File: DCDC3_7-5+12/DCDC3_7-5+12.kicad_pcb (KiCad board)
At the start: 2 copper layers, 63.5 x 75.8 mm, 34 parts, among them J1 FAN, Q1 CSD16323Q3, T1 + 3.7V -, T2 + 12V -, T3 + 5V -, U1 LM3488, U2 XL6009

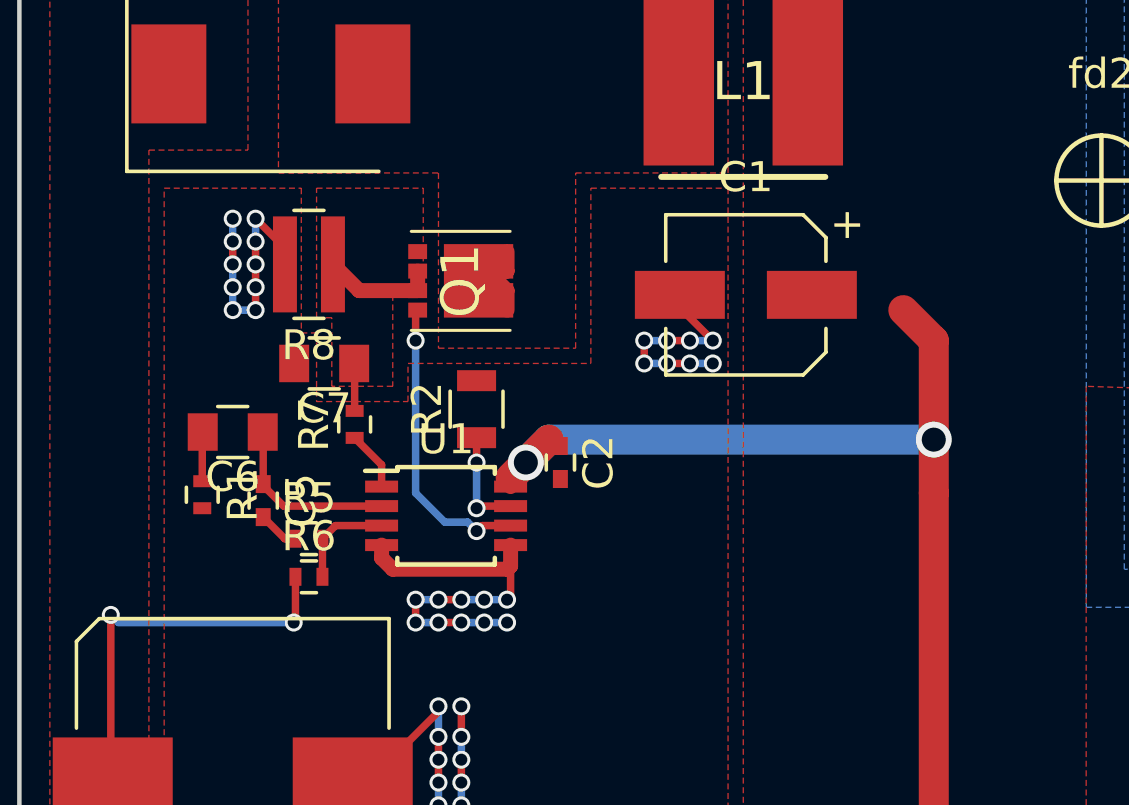
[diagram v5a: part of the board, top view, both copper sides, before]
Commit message: Final version of aux 5v and 12v power supply.
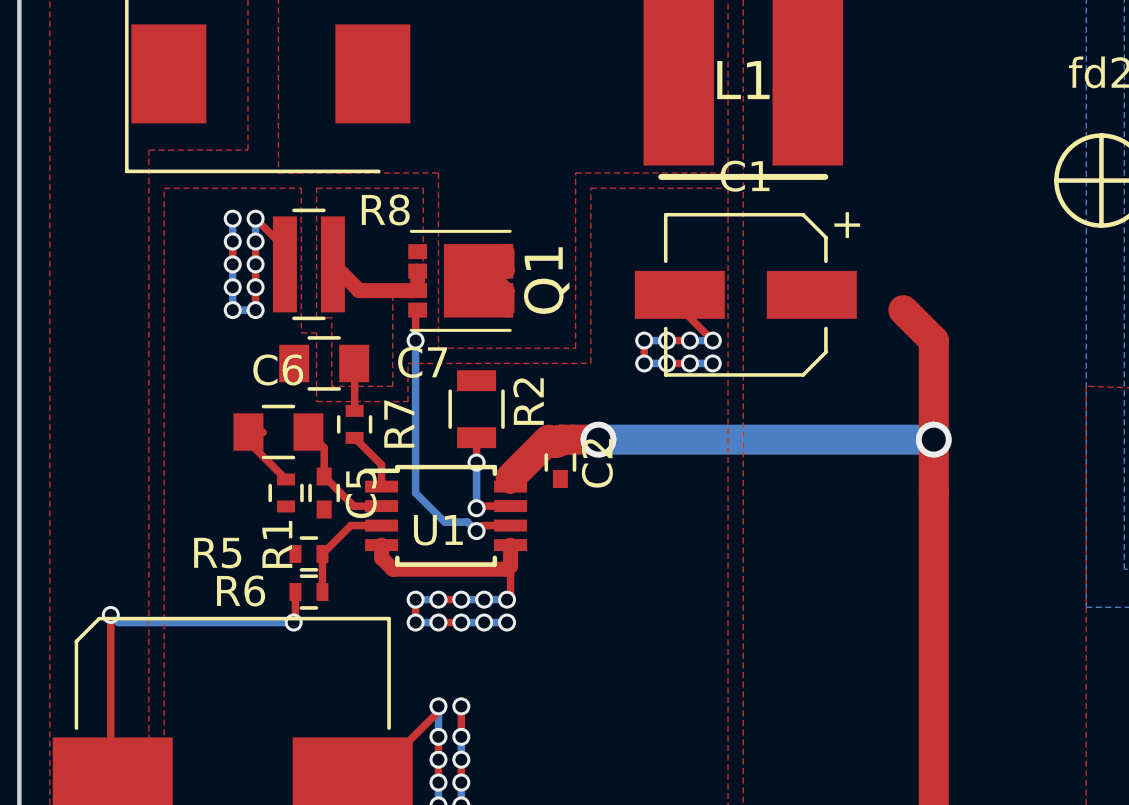
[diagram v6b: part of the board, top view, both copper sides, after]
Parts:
- moved R1 2.79 mm to (110.5, 105.4)
- moved C5 2.05 mm to (111.8, 105.4)
- moved C6 1.52 mm to (110.2, 103.4)
- moved R6 0.51 mm to (111.3, 108.7)
- moved R5 0.51 mm to (111.3, 107.4)
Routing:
- net Net-(C5-Pad1): track 6.02 -> 4.02 mm
- net GND: track 75.9 -> 74.5 mm
- net /DCDC 3.7 - 12/3.7V: track 93.6 -> 92.8 mm
- net /DCDC 3.7 - 12/12V: track 13.1 -> 12.6 mm
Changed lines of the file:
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@@
 (kicad_pcb (version 4) (host pcbnew 4.0.7+dfsg1-1ubuntu2)
   (general
-    (links 0)
+    (links 62)
     (no_connects 0)
     (area 101.524999 63.424999 165.175001 139.375001)
     (thickness 1.6)
     (drawings 12)
-    (tracks 204)
+    (tracks 207)
     (zones 0)
     (modules 34)
@@
   )
   (module Resistors_SMD:R_0402 (layer F.Cu)
-    (at 107.696 105.468 270)
+    (at 110.49 105.41 270)
     (descr "Resistor SMD 0402, reflow soldering, Vishay (see dcrcw.pdf)")
     (tags "resistor 0402")
     (attr smd)
-    (fp_text reference R1 (at 0 -1.35 270) (layer F.SilkS)
+    (fp_text reference R1 (at 1.72 0.254 270) (layer F.SilkS)
       (effects (font (size 1 1) (thickness 0.15)))
     )
@@
     (tags "MOSFET (N-Channel)")
     (attr smd)
-    (fp_text reference Q1 (at 0 0 270) (layer F.SilkS)
+    (fp_text reference Q1 (at -0.041 -2.815 270) (layer F.SilkS)
       (effects (font (size 1.27 1.27) (thickness 0.254)))
     )
@@
   )
   (module Capacitors_SMD:C_0402 (layer F.Cu)
-    (at 109.728 105.664 270)
+    (at 111.76 105.41 270)
     (descr "Capacitor SMD 0402, reflow soldering, AVX (see smccp.pdf)")
     (tags "capacitor 0402")
@@
   )
   (module Capacitors_SMD:C_0805 (layer F.Cu)
-    (at 108.712 103.378 180)
+    (at 110.236 103.378 180)
     (descr "Capacitor SMD 0805, reflow soldering, AVX (see smccp.pdf)")
     (tags "capacitor 0805")
     (attr smd)
-    (fp_text reference C6 (at 0 -1.5 180) (layer F.SilkS)
+    (fp_text reference C6 (at 0 2.032 180) (layer F.SilkS)
       (effects (font (size 1 1) (thickness 0.15)))
     )
@@
     (tags "capacitor 0805")
     (attr smd)
-    (fp_text reference C7 (at 0 -1.5 180) (layer F.SilkS)
+    (fp_text reference C7 (at -3.302 0 180) (layer F.SilkS)
       (effects (font (size 1 1) (thickness 0.15)))
     )
@@
     (tags "resistor 0805")
     (attr smd)
-    (fp_text reference R2 (at 0 -1.65 90) (layer F.SilkS)
+    (fp_text reference R2 (at 0.254 1.778 90) (layer F.SilkS)
       (effects (font (size 1 1) (thickness 0.15)))
     )
@@
   )
   (module Resistors_SMD:R_0402 (layer F.Cu)
-    (at 111.252 106.934)
+    (at 111.252 107.442)
     (descr "Resistor SMD 0402, reflow soldering, Vishay (see dcrcw.pdf)")
     (tags "resistor 0402")
     (attr smd)
-    (fp_text reference R5 (at 0 -1.35) (layer F.SilkS)
+    (fp_text reference R5 (at -3.048 0) (layer F.SilkS)
       (effects (font (size 1 1) (thickness 0.15)))
     )
@@
   )
   (module Resistors_SMD:R_0402 (layer F.Cu)
-    (at 111.252 108.204)
+    (at 111.252 108.712)
     (descr "Resistor SMD 0402, reflow soldering, Vishay (see dcrcw.pdf)")
     (tags "resistor 0402")
     (attr smd)
-    (fp_text reference R6 (at 0 -1.35) (layer F.SilkS)
+    (fp_text reference R6 (at -2.286 0) (layer F.SilkS)
       (effects (font (size 1 1) (thickness 0.15)))
     )
@@
     (tags "resistor 0402")
     (attr smd)
-    (fp_text reference R7 (at 0 -1.35 90) (layer F.SilkS)
+    (fp_text reference R7 (at 0 1.524 90) (layer F.SilkS)
       (effects (font (size 1 1) (thickness 0.15)))
     )
@@
     (tags "resistor 0612 ")
     (attr smd)
-    (fp_text reference R8 (at 0 -2.7 180) (layer F.SilkS)
+    (fp_text reference R8 (at -2.54 1.778 180) (layer F.SilkS)
       (effects (font (size 1 1) (thickness 0.15)))
     )
@@
     (tags "SSOP 0.65")
     (attr smd)
-    (fp_text reference U1 (at 0 -2.55) (layer F.SilkS)
+    (fp_text reference U1 (at -0.254 0.508) (layer F.SilkS)
       (effects (font (size 1 1) (thickness 0.15)))
     )
@@
   (gr_line (start 165.1 63.5) (end 165.1 139.3) (layer Edge.Cuts) (width 0.15))
   (gr_line (start 101.6 63.5) (end 165.1 63.5) (layer Edge.Cuts) (width 0.15))
-  (segment (start 119.244 103.632) (end 118.482 104.394) (width 1) (layer F.Cu) (net 1))
-  (segment (start 118.482 104.394) (end 117.974 104.902) (width 1) (layer F.Cu) (net 1))
-  (segment (start 119.244 103.632) (end 118.482 104.394) (width 1) (layer B.Cu) (net 1))
-  (segment (start 132.08 103.632) (end 119.244 103.632) (width 1) (layer B.Cu) (net 1))
-  (via (at 118.482 104.394) (size 1.2) (drill 0.8) (layers F.Cu B.Cu) (net 1))
+  (segment (start 120.904006 103.632) (end 120.904 103.632006) (width 1) (layer B.Cu) (net 1))
+  (segment (start 119.633994 103.632006) (end 120.055472 103.632006) (width 1) (layer F.Cu) (net 1))
+  (segment (start 132.08 103.632) (end 120.904006 103.632) (width 1) (layer B.Cu) (net 1))
+  (via (at 120.904 103.632006) (size 1.2) (drill 0.8) (layers F.Cu B.Cu) (net 1))
+  (segment (start 117.974 104.902) (end 119.152001 103.723999) (width 1) (layer F.Cu) (net 1))
+  (segment (start 120.055472 103.632006) (end 120.904 103.632006) (width 1) (layer F.Cu) (net 1))
+  (segment (start 119.542001 103.723999) (end 119.633994 103.632006) (width 1) (layer F.Cu) (net 1))
+  (segment (start 119.152001 103.723999) (end 119.542001 103.723999) (width 1) (layer F.Cu) (net 1))
+  (segment (start 119.335999 103.723999) (end 119.542001 103.723999) (width 1) (layer F.Cu) (net 1))
+  (segment (start 119.244 103.632) (end 119.335999 103.723999) (width 1) (layer F.Cu) (net 1))
   (via (at 132.08 103.632) (size 1.2) (drill 0.8) (layers F.Cu B.Cu) (net 1))
   (segment (start 119.634 103.844) (end 119.456 103.844) (width 0.25) (layer F.Cu) (net 1))
@@
   (segment (start 148.33 95.68) (end 145.03 95.68) (width 1) (layer F.Cu) (net 1))
   (segment (start 145.03 95.68) (end 144.78 95.93) (width 1) (layer F.Cu) (net 1))
+  (segment (start 110.802 108.712) (end 110.802 109.67) (width 0.25) (layer F.Cu) (net 2))
+  (segment (start 110.802 109.67) (end 110.744 109.728) (width 0.25) (layer F.Cu) (net 2))
   (segment (start 104.648 109.474) (end 104.648 114.744) (width 0.25) (layer F.Cu) (net 2))
   (segment (start 104.648 114.744) (end 104.712 114.808) (width 0.25) (layer F.Cu) (net 2))
@@
   (segment (start 104.902 109.728) (end 104.648 109.474) (width 0.25) (layer B.Cu) (net 2))
   (via (at 104.648 109.474) (size 0.6) (drill 0.4) (layers F.Cu B.Cu) (net 2))
-  (segment (start 110.802 108.204) (end 110.802 109.67) (width 0.25) (layer F.Cu) (net 2))
-  (segment (start 110.802 109.67) (end 110.744 109.728) (width 0.25) (layer F.Cu) (net 2))
   (via (at 110.744 109.728) (size 0.6) (drill 0.4) (layers F.Cu B.Cu) (net 2))
   (segment (start 153.67 133.35) (end 153.67 128.27) (width 1) (layer F.Cu) (net 3))
@@
   (segment (start 110.452 97.244) (end 109.474 96.266) (width 0.25) (layer F.Cu) (net 6))
   (via (at 109.474 96.266) (size 0.6) (drill 0.4) (layers F.Cu B.Cu) (net 6))
-  (segment (start 110.802 106.934) (end 110.448 106.934) (width 0.25) (layer F.Cu) (net 6))
-  (segment (start 110.448 106.934) (end 109.728 106.214) (width 0.25) (layer F.Cu) (net 6))
   (segment (start 113.674 107.147) (end 113.674 107.578) (width 0.5) (layer F.Cu) (net 6))
   (segment (start 117.871 107.95) (end 117.974 107.847) (width 0.5) (layer F.Cu) (net 6))
@@
   (segment (start 148.59 93.98) (end 148.33 93.98) (width 1) (layer F.Cu) (net 6))
   (segment (start 148.33 93.98) (end 148.33 93.72) (width 1) (layer F.Cu) (net 6))
-  (segment (start 109.728 105.114) (end 109.728 103.394) (width 0.25) (layer F.Cu) (net 7))
-  (segment (start 109.728 103.394) (end 109.712 103.378) (width 0.25) (layer F.Cu) (net 7))
-  (segment (start 113.674 105.847) (end 110.411 105.847) (width 0.25) (layer F.Cu) (net 7))
-  (segment (start 110.411 105.847) (end 109.728 105.164) (width 0.25) (layer F.Cu) (net 7))
-  (segment (start 109.728 105.164) (end 109.728 105.114) (width 0.25) (layer F.Cu) (net 7))
-  (segment (start 107.696 105.018) (end 107.696 103.394) (width 0.25) (layer F.Cu) (net 8))
-  (segment (start 107.696 103.394) (end 107.712 103.378) (width 0.25) (layer F.Cu) (net 8))
+  (segment (start 111.76 104.86) (end 112.747 105.847) (width 0.25) (layer F.Cu) (net 7))
+  (segment (start 112.747 105.847) (end 113.674 105.847) (width 0.25) (layer F.Cu) (net 7))
+  (segment (start 111.76 104.86) (end 111.76 103.902) (width 0.25) (layer F.Cu) (net 7))
+  (segment (start 111.76 103.902) (end 111.236 103.378) (width 0.25) (layer F.Cu) (net 7))
+  (segment (start 109.728 103.394) (end 109.712 103.378) (width 0.25) (layer F.Cu) (net 8))
+  (segment (start 110.49 104.96) (end 109.236 103.706) (width 0.25) (layer F.Cu) (net 8))
+  (segment (start 109.236 103.706) (end 109.236 103.378) (width 0.25) (layer F.Cu) (net 8))
   (segment (start 114.876 98.664) (end 112.926 98.664) (width 0.5) (layer F.Cu) (net 9))
   (segment (start 112.926 98.664) (end 112.052 97.79) (width 0.5) (layer F.Cu) (net 9))
@@
   (segment (start 116.911 105.847) (end 116.84 105.918) (width 0.25) (layer F.Cu) (net 12))
   (via (at 116.84 105.918) (size 0.6) (drill 0.4) (layers F.Cu B.Cu) (net 12))
-  (segment (start 111.702 106.934) (end 111.702 108.204) (width 0.25) (layer F.Cu) (net 13))
-  (segment (start 113.674 106.497) (end 112.139 106.497) (width 0.25) (layer F.Cu) (net 13))
-  (segment (start 112.139 106.497) (end 111.702 106.934) (width 0.25) (layer F.Cu) (net 13))
+  (segment (start 111.702 107.442) (end 112.647 106.497) (width 0.25) (layer F.Cu) (net 13))
+  (segment (start 112.647 106.497) (end 113.674 106.497) (width 0.25) (layer F.Cu) (net 13))
+  (segment (start 111.702 108.712) (end 111.702 107.442) (width 0.25) (layer F.Cu) (net 13))
   (segment (start 113.674 105.197) (end 113.674 104.472) (width 0.25) (layer F.Cu) (net 14))
   (segment (start 113.674 104.472) (end 112.776 103.574) (width 0.25) (layer F.Cu) (net 14))

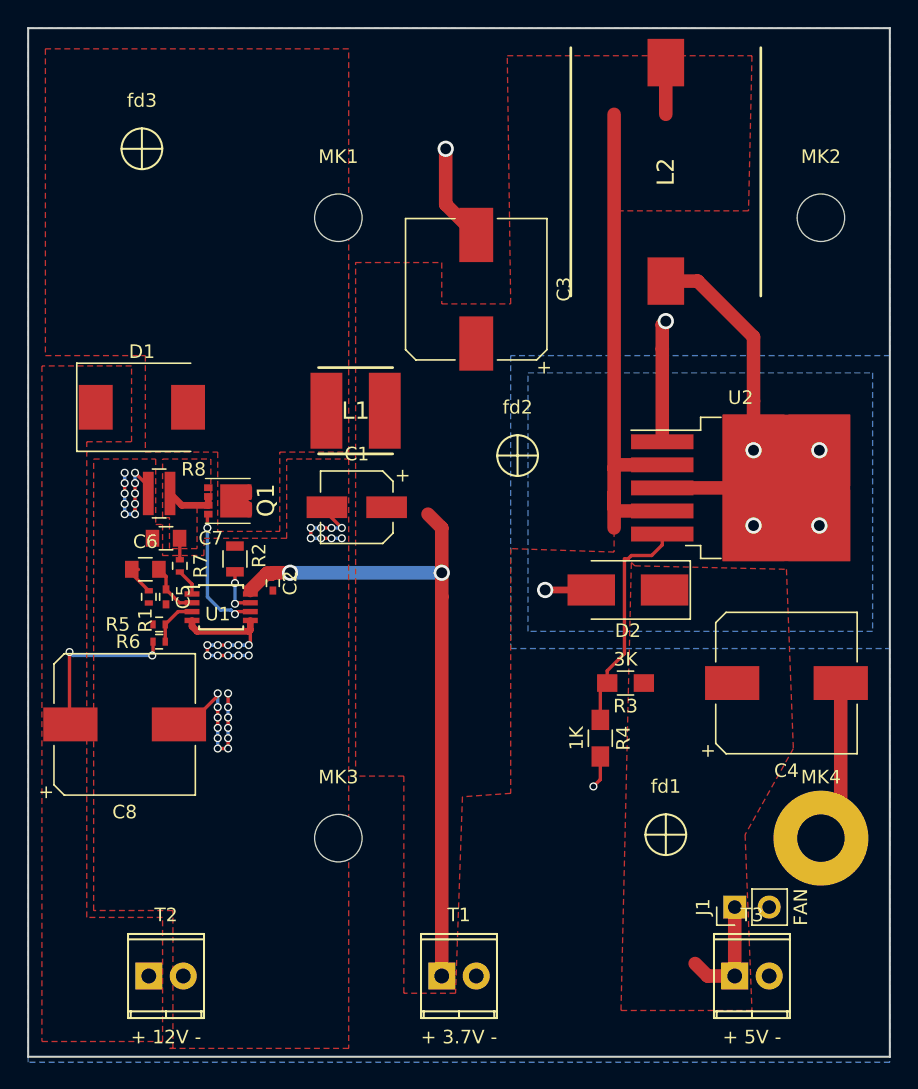
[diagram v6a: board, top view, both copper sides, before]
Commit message: Final version of aux 5v and 12v power supply.
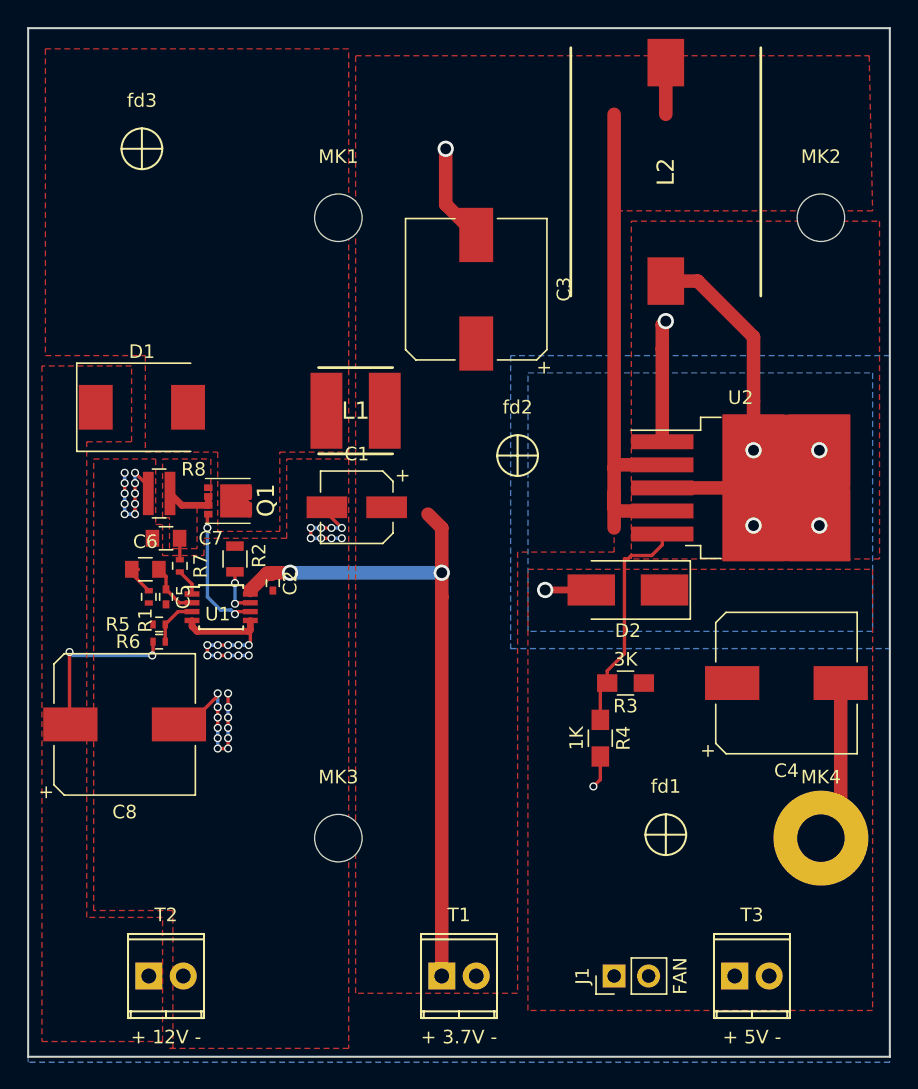
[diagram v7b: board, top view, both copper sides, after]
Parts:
- moved J1 10.2 mm to (144.8, 133.3)
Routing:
- net /DCDC 3.7 to 5/5V: track 8.38 -> 0.00 mm
- added copper zone on F.Cu, net Net-(D2-Pad2)
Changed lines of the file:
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@@
     (links 62)
     (no_connects 0)
-    (area 101.524999 63.424999 165.175001 139.375001)
+    (area 93.769977 54.45 183.11 139.700001)
     (thickness 1.6)
     (drawings 12)
-    (tracks 207)
+    (tracks 204)
     (zones 0)
     (modules 34)
@@
   )
   (module Pin_Headers:Pin_Header_Straight_1x02_Pitch2.54mm (layer F.Cu)
-    (at 153.67 128.27 90)
+    (at 144.78 133.35 90)
     (descr "Through hole straight pin header, 1x02, 2.54mm pitch, single row")
     (tags "Through hole pin header THT 1x02 2.54mm single row")
@@
   (via (at 104.648 109.474) (size 0.6) (drill 0.4) (layers F.Cu B.Cu) (net 2))
   (via (at 110.744 109.728) (size 0.6) (drill 0.4) (layers F.Cu B.Cu) (net 2))
-  (segment (start 153.67 133.35) (end 153.67 128.27) (width 1) (layer F.Cu) (net 3))
-  (segment (start 150.75 132.42949) (end 151.67051 133.35) (width 1) (layer F.Cu) (net 3))
-  (segment (start 151.67051 133.35) (end 153.67 133.35) (width 1) (layer F.Cu) (net 3))
   (segment (start 143.096 104.902) (end 139.7 104.902) (width 0.5) (layer F.Cu) (net 4))
   (via (at 139.7 104.902) (size 1.2) (drill 0.8) (layers F.Cu B.Cu) (net 4))
@@
     (polygon
       (pts
-        (xy 125.73 86.614) (xy 125.73 80.772) (xy 132.08 80.772) (xy 132.08 83.82) (xy 137.16 83.82)
-        (xy 136.906 65.532) (xy 154.94 65.532) (xy 154.686 76.962) (xy 144.78 76.962) (xy 144.78 83.566)
-        (xy 144.78 102.108) (xy 137.16 101.854) (xy 137.16 119.888) (xy 133.604 120.142) (xy 133.096 134.62)
-        (xy 129.286 134.62) (xy 129.286 118.618) (xy 125.73 118.618)
+        (xy 125.73 65.532) (xy 163.576 65.532) (xy 163.83 76.962) (xy 144.78 76.962) (xy 144.78 102.108)
+        (xy 137.668 102.108) (xy 137.668 134.62) (xy 125.73 134.62)
       )
     )
@@
     (polygon
       (pts
-        (xy 146.304 103.124) (xy 157.48 103.378) (xy 157.988 116.586) (xy 154.432 122.936) (xy 154.94 135.89)
-        (xy 145.288 135.89) (xy 146.05 102.87) (xy 146.05 102.87)
+        (xy 163.83 103.378) (xy 163.83 135.89) (xy 138.43 135.89) (xy 138.43 103.378)
       )
     )
@@
       )
     )
+  )
+  (zone (net 4) (net_name "Net-(D2-Pad2)") (layer F.Cu) (hatch edge 0.508)
+    (connect_pads yes (clearance 0.508))
+    (min_thickness 0.254)
+    (fill yes (arc_segments 16) (thermal_gap 0.508) (thermal_bridge_width 0.508))
+    (polygon
+      (pts
+        (xy 146.05 77.724) (xy 164.338 77.724) (xy 164.338 102.616) (xy 146.05 102.616)
+      )
+    )
